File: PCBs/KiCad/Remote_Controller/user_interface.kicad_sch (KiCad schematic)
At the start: 0 parts

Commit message: Numbered all of the schematics
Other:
- note added: "[3] User Interface"
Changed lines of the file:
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@@
 	(generator_version "8.0")
 	(paper "A4")
+	(text "[3] User Interface\n"
+		(exclude_from_sim no)
+		(at 52.578 20.828 0)
+		(effects
+			(font
+				(size 5.08 5.08)
+				(thickness 1.016)
+				(bold yes)
+			)
+		)
+	)
 )

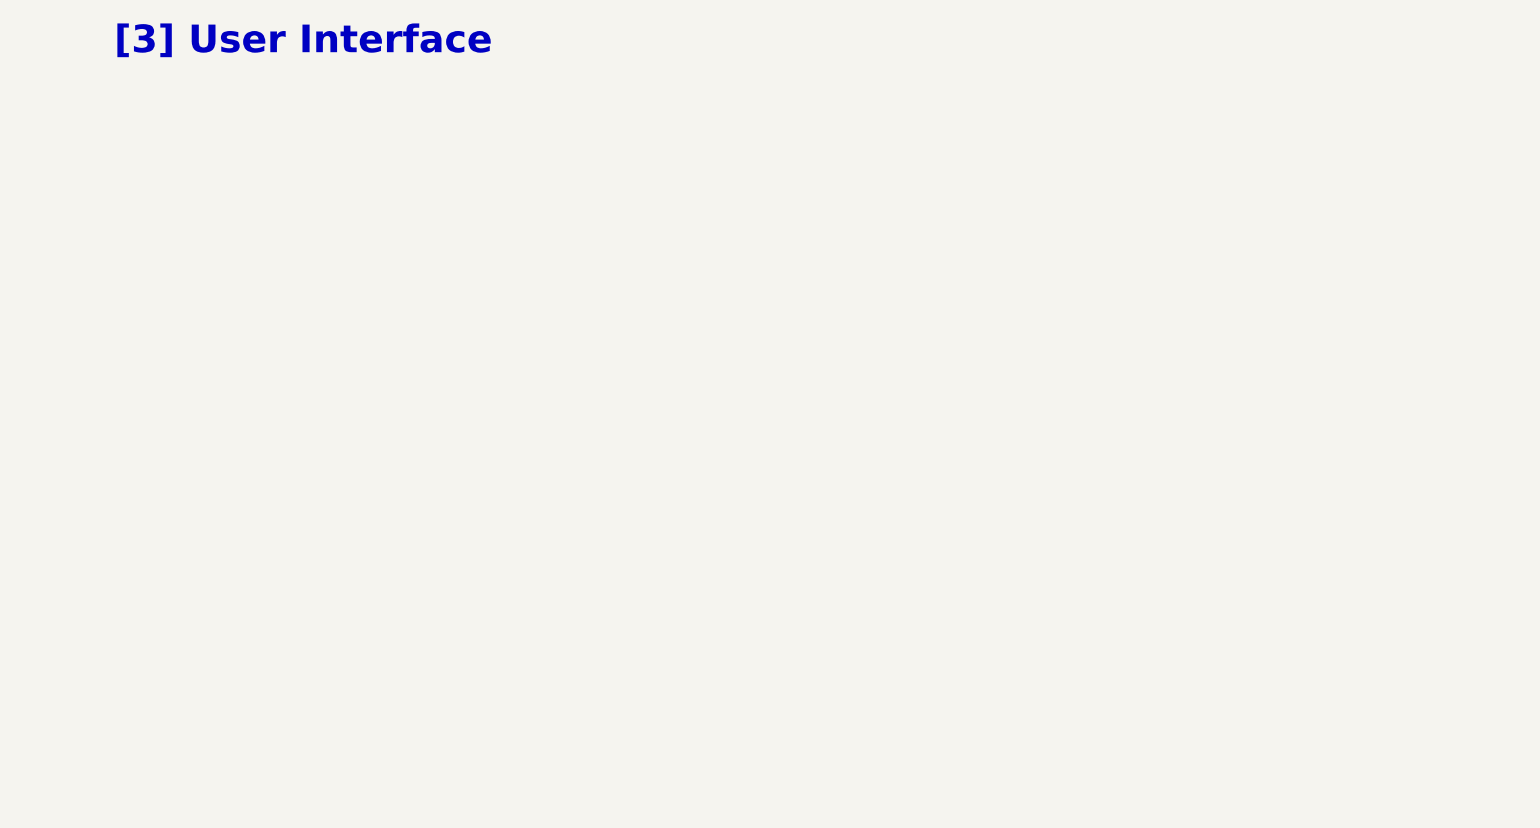
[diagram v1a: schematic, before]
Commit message: Add LCD screen symbol to project library, and add LCD screen and function buttons to user interface schematic
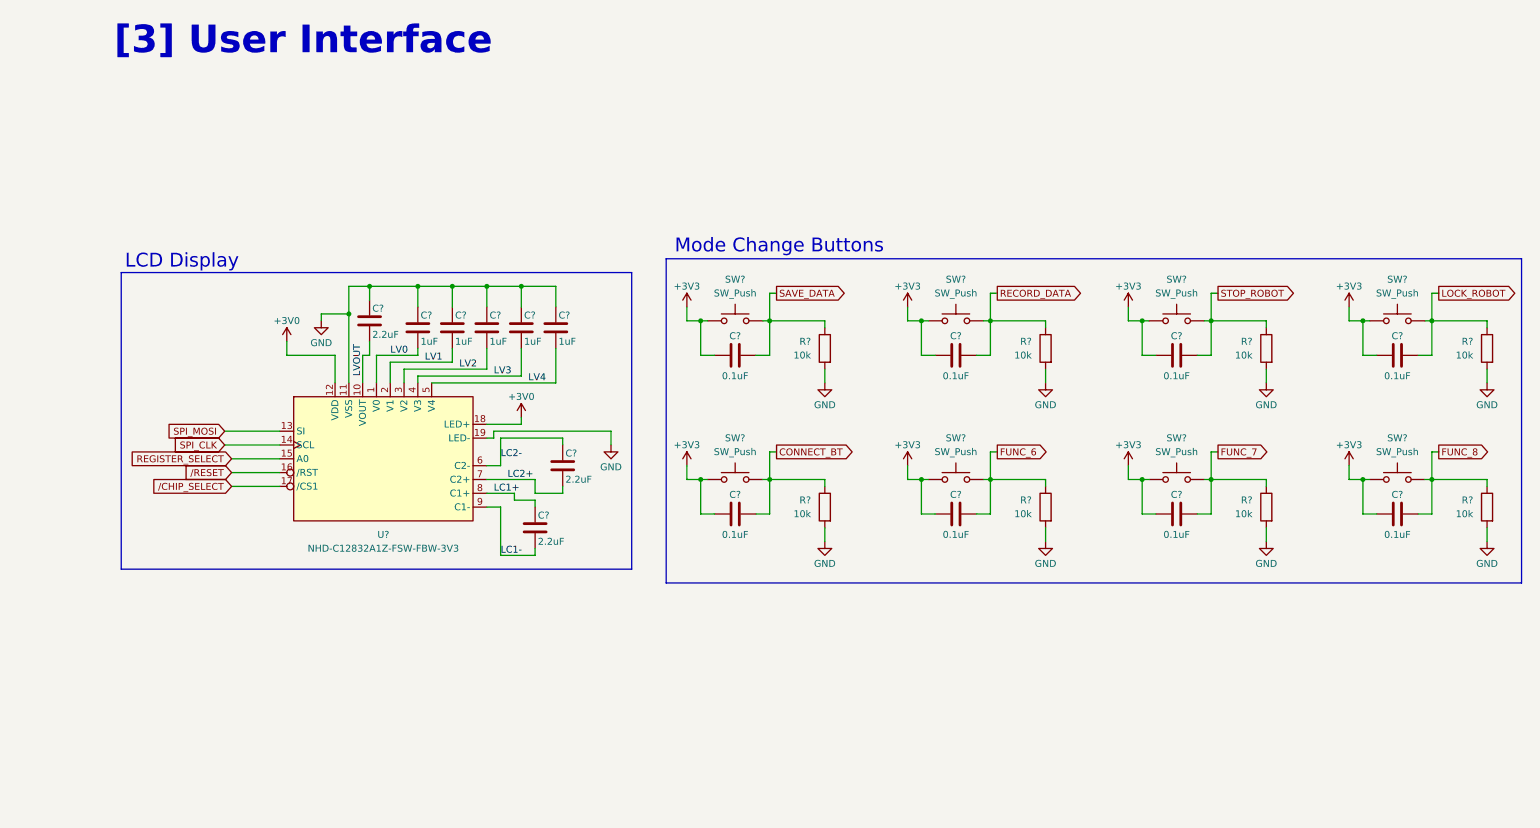
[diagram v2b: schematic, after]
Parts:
- added C? (x8): 0.1uF, symbol Device:C
- added C? (x5): 1uF, Capacitor_SMD:C_0402_1005Metric, symbol Device:C
- added C? (x3): 2.2uF, Capacitor_SMD:C_0402_1005Metric, symbol Device:C
- added R? (x8): 10k, symbol Device:R
- added SW? (x8): SW_Push, symbol Switch:SW_Push
- added U?: NHD-C12832A1Z-FSW-FBW-3V3, symbol NHD-C12832A1Z-FSW-FBW-3V3:NHD-C12832A1Z-FSW-FBW-3V3
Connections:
- new net +3V0: U?.12 (VDD), U?.18 (LED+)
- new net +3V3: C?.2, C?.2, C?.2, C?.2, C?.2, C?.2, C?.2, C?.2, SW?.2, SW?.2, SW?.2, SW?.2, SW?.2, SW?.2, SW?.2, SW?.2
- new net CONNECT_BT: C?.1, R?.1, SW?.1
- new net FUNC_6: C?.1, R?.1, SW?.1
- new net FUNC_7: C?.1, R?.1, SW?.1
- new net FUNC_8: C?.1, R?.1, SW?.1
- new net GND: C?.1, C?.1, C?.1, C?.1, C?.1, C?.1, R?.2, R?.2, R?.2, R?.2, R?.2, R?.2, R?.2, R?.2, U?.11 (VSS), U?.19 (LED-)
- new net LC1+: C?.1, U?.8 (C1+)
- new net LC1-: C?.2, U?.9 (C1-)
- new net LC2+: C?.2, U?.7 (C2+)
- new net LC2-: C?.1, U?.6 (C2-)
- new net LOCK_ROBOT: C?.1, R?.1, SW?.1
- new net LV0: C?.2, U?.1 (V0)
- new net LV1: C?.2, U?.2 (V1)
- new net LV2: C?.2, U?.3 (V2)
- new net LV3: C?.2, U?.4 (V3)
- new net LV4: C?.2, U?.5 (V4)
- new net LVOUT: C?.2, U?.10 (VOUT)
- new net RECORD_DATA: C?.1, R?.1, SW?.1
- new net REGISTER_SELECT: U?.15 (A0)
- new net SAVE_DATA: C?.1, R?.1, SW?.1
- new net SPI_CLK: U?.14 (SCL)
- new net SPI_MOSI: U?.13 (SI)
- new net STOP_ROBOT: C?.1, R?.1, SW?.1
- new net /CHIP_SELECT: U?.17 (/CS1)
- new net /RESET: U?.16 (/RST)
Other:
- note added: "LCD Display"
- note added: "Mode Change Buttons"

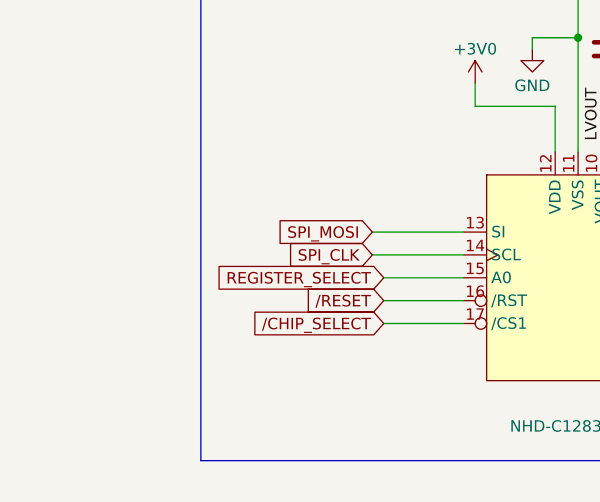
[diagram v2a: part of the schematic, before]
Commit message: Corrected uC-screen connection names
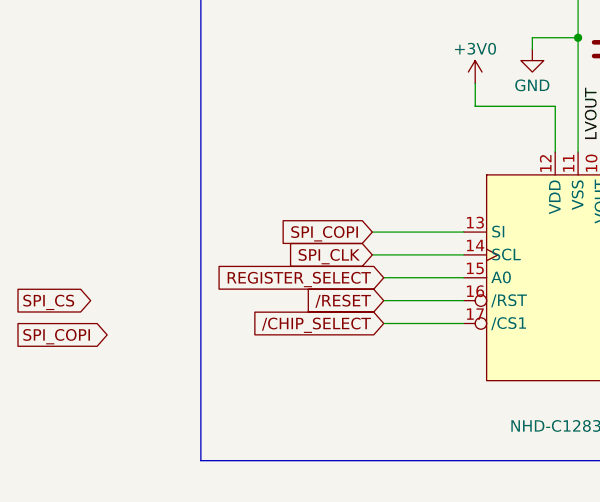
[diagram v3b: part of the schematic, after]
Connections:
- net SPI_MOSI renamed SPI_COPI
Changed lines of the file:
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@@
+		)
+	)
+	(global_label "SPI_CS"
+		(shape output)
+		(at -1.27 100.33 0)
+		(fields_autoplaced yes)
+		(effects
+			(font
+				(size 1.27 1.27)
+			)
+			(justify left)
+		)
+		(property "Intersheetrefs" "${INTERSHEET_REFS}"
+			(at 8.2466 100.33 0)
+			(effects
+				(font
+					(size 1.27 1.27)
+				)
+				(justify left)
+				(hide yes)
+			)
 		)
 	)
@@
 		)
 	)
-	(global_label "SPI_MOSI"
+	(global_label "SPI_COPI"
 		(shape input)
 		(at 38.1 92.71 180)
@@
 		)
 		(property "Intersheetrefs" "${INTERSHEET_REFS}"
-			(at 26.4667 92.71 0)
+			(at 26.5876 92.71 0)
 			(effects
 				(font
@@
 				(hide yes)
 			)
+		)
+	)
+	(global_label "SPI_COPI"
+		(shape output)
+		(at -1.27 104.14 0)
+		(fields_autoplaced yes)
+		(effects
+			(font
+				(size 1.27 1.27)
+			)
+			(justify left)
+		)
+		(property "Intersheetrefs" "${INTERSHEET_REFS}"
+			(at 10.2424 104.14 0)
+			(effects
+				(font
+					(size 1.27 1.27)
+				)
+				(justify left)
+				(hide yes)
+			)

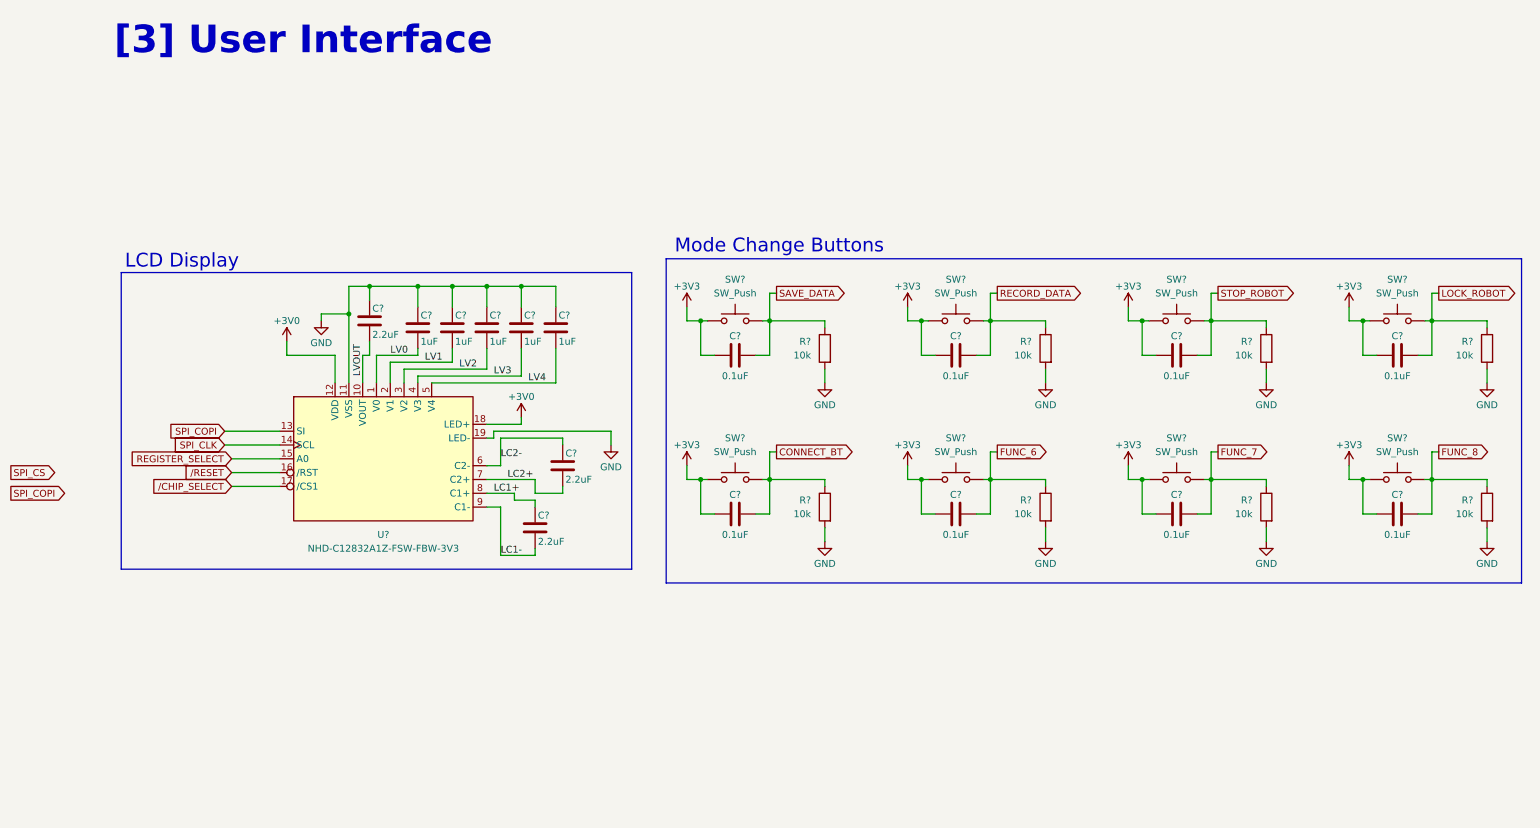
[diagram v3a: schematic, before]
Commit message: Added Thumb joystick symbols, and finish UI schematic with joysticks to control rotational and linear velocity
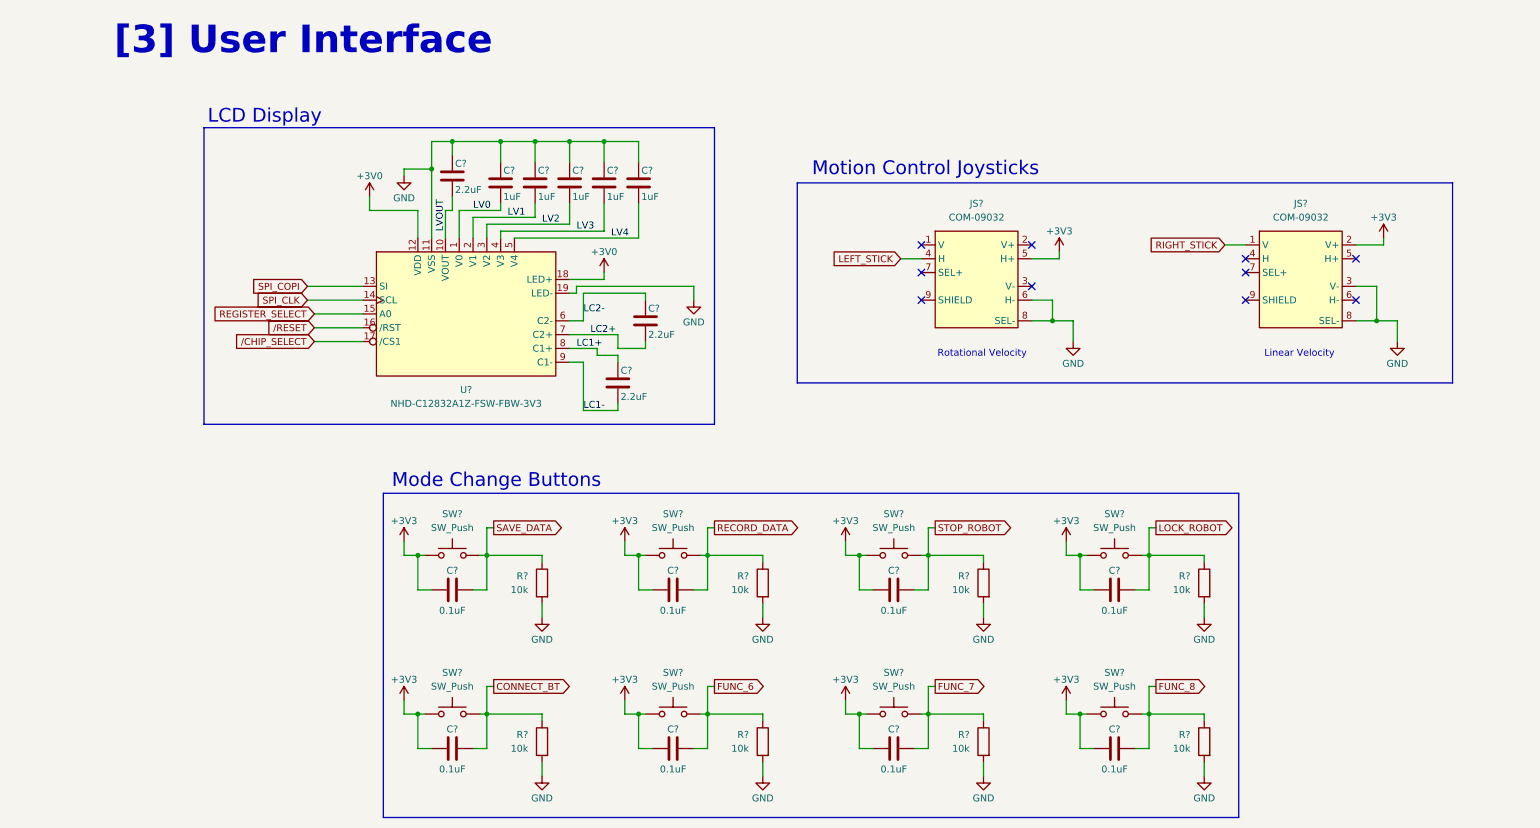
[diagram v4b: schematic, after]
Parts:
- added JS? (x2): COM-09032, symbol Thumb_Joystick:Joystick
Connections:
- net +3V3: now also JS?.2 (V+), JS?.5 (H+)
- net GND: now also JS?.3 (V-), JS?.6 (H-), JS?.8 (SEL-), JS?.8 (SEL-)
- new net LEFT_STICK: JS?.4 (H)
- new net RIGHT_STICK: JS?.1 (V)
- no-connect marks 0 -> 10
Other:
- note added: "Linear Velocity"
- note added: "Motion Control Joysticks"
- note added: "Rotational Velocity"
- moved on the sheet: C?, R?, SW?, U?

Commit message: Labeled all nets, corrected some labels, added battery-cell symbol
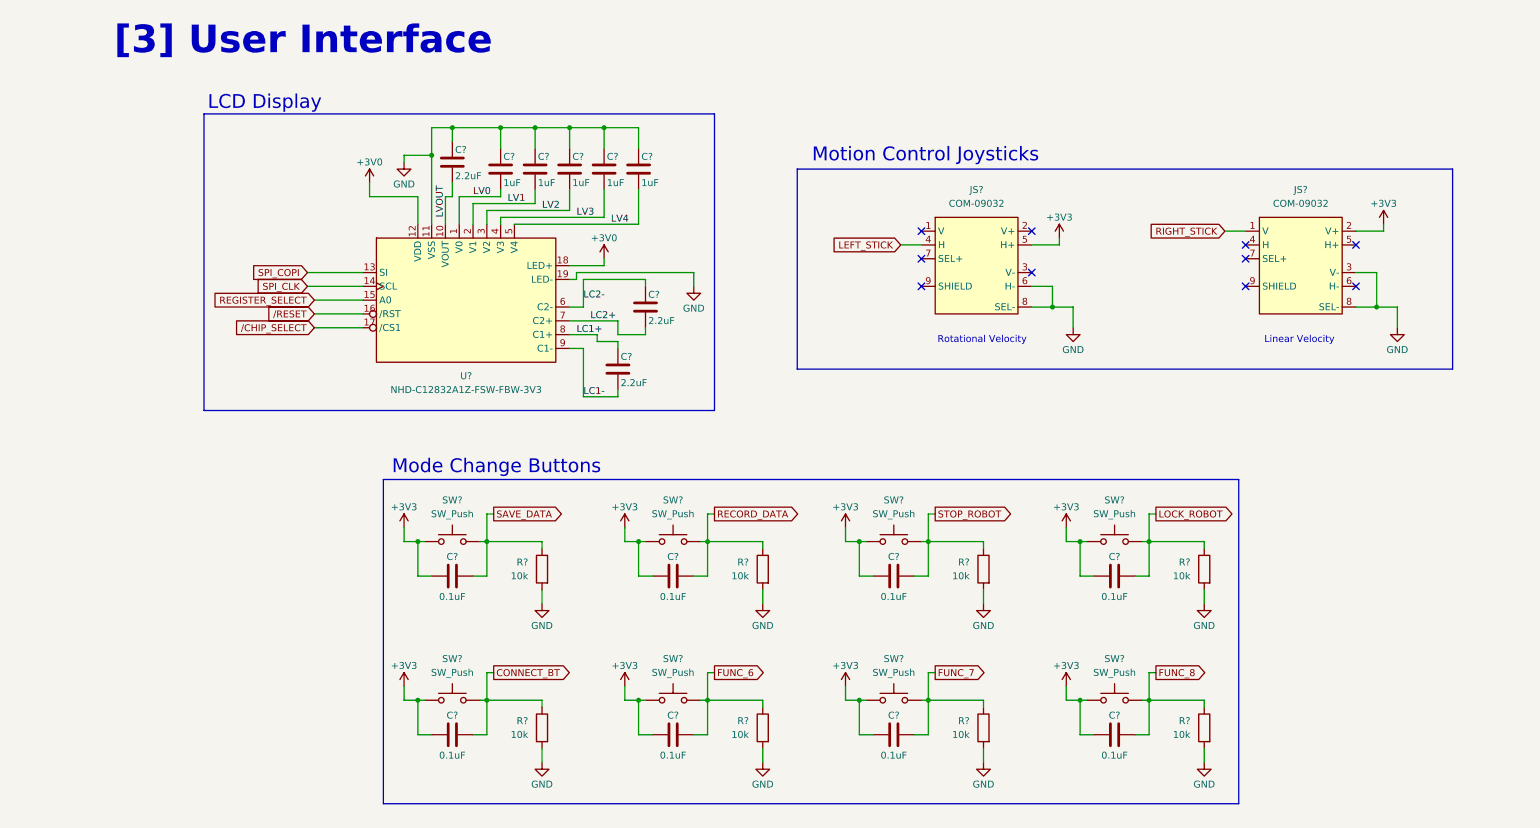
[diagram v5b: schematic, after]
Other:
- moved on the sheet: C?, JS?, R?, SW?, U?

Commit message: Annotate components
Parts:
- gave numbers to parts that had none: 35

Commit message: Add footprints except connectors, buttons and switches
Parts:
- C309, C310, C311, C312, C313, C314, C315, C316: footprint (none) -> Capacitor_SMD:C_0402_1005Metric
- R301, R302, R303, R304, R305, R306, R307, R308: footprint (none) -> Resistor_SMD:R_0402_1005Metric
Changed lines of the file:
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@@
 			)
 		)
-		(property "Footprint" ""
+		(property "Footprint" "Resistor_SMD:R_0402_1005Metric"
 			(at 98.298 118.11 90)
 			(effects
@@
 			)
 		)
-		(property "Footprint" ""
+		(property "Footprint" "Capacitor_SMD:C_0402_1005Metric"
 			(at 76.2 118.4148 0)
 			(effects
@@
 			)
 		)
-		(property "Footprint" ""
+		(property "Footprint" "Capacitor_SMD:C_0402_1005Metric"
 			(at 198.12 147.6248 0)
 			(effects
@@
 			)
 		)
-		(property "Footprint" ""
+		(property "Footprint" "Resistor_SMD:R_0402_1005Metric"
 			(at 179.578 147.32 90)
 			(effects
@@
 			)
 		)
-		(property "Footprint" ""
+		(property "Footprint" "Capacitor_SMD:C_0402_1005Metric"
 			(at 116.84 147.6248 0)
 			(effects
@@
 			)
 		)
-		(property "Footprint" ""
+		(property "Footprint" "Capacitor_SMD:C_0402_1005Metric"
 			(at 157.48 147.6248 0)
 			(effects
@@
 			)
 		)
-		(property "Footprint" ""
+		(property "Footprint" "Capacitor_SMD:C_0402_1005Metric"
 			(at 157.48 118.4148 0)
 			(effects
@@
 			)
 		)
-		(property "Footprint" ""
+		(property "Footprint" "Resistor_SMD:R_0402_1005Metric"
 			(at 138.938 118.11 90)
 			(effects
@@
 			)
 		)
-		(property "Footprint" ""
+		(property "Footprint" "Resistor_SMD:R_0402_1005Metric"
 			(at 98.298 147.32 90)
 			(effects
@@
 			)
 		)
-		(property "Footprint" ""
+		(property "Footprint" "Capacitor_SMD:C_0402_1005Metric"
 			(at 198.12 118.4148 0)
 			(effects
@@
 			)
 		)
-		(property "Footprint" ""
+		(property "Footprint" "Capacitor_SMD:C_0402_1005Metric"
 			(at 116.84 118.4148 0)
 			(effects
@@
 			)
 		)
-		(property "Footprint" ""
+		(property "Footprint" "Resistor_SMD:R_0402_1005Metric"
 			(at 220.218 147.32 90)
 			(effects
@@
 			)
 		)
-		(property "Footprint" ""
+		(property "Footprint" "Capacitor_SMD:C_0402_1005Metric"
 			(at 76.2 147.6248 0)
 			(effects
@@
 			)
 		)
-		(property "Footprint" ""
+		(property "Footprint" "Resistor_SMD:R_0402_1005Metric"
 			(at 179.578 118.11 90)
 			(effects
@@
 			)
 		)
-		(property "Footprint" ""
+		(property "Footprint" "Resistor_SMD:R_0402_1005Metric"
 			(at 138.938 147.32 90)
 			(effects
@@
 			)
 		)
-		(property "Footprint" ""
+		(property "Footprint" "Resistor_SMD:R_0402_1005Metric"
 			(at 220.218 118.11 90)
 			(effects

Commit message: Add USB receptacle and LCD footprints
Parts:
- U301: footprint (none) -> Display:NHD-C12832A1Z-FSRGB
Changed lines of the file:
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@@
 			)
 		)
-		(property "Footprint" ""
+		(property "Footprint" "Display:NHD-C12832A1Z-FSRGB"
 			(at 81.28 54.61 90)
 			(effects
